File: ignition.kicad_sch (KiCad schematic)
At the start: 5 parts, among them J2 Centroid, Q1 Q_NMOS_GDS

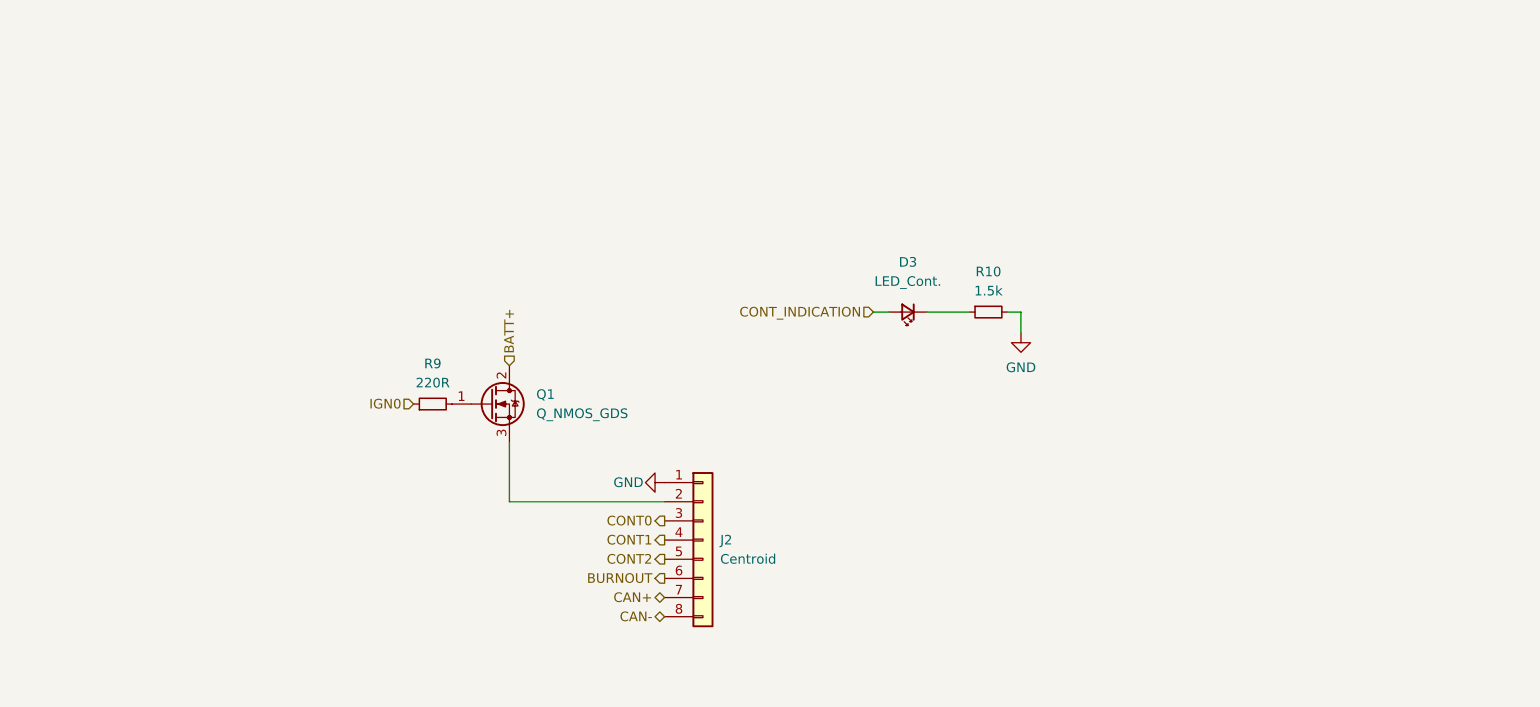
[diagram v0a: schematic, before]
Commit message: Update ignition system with CDI
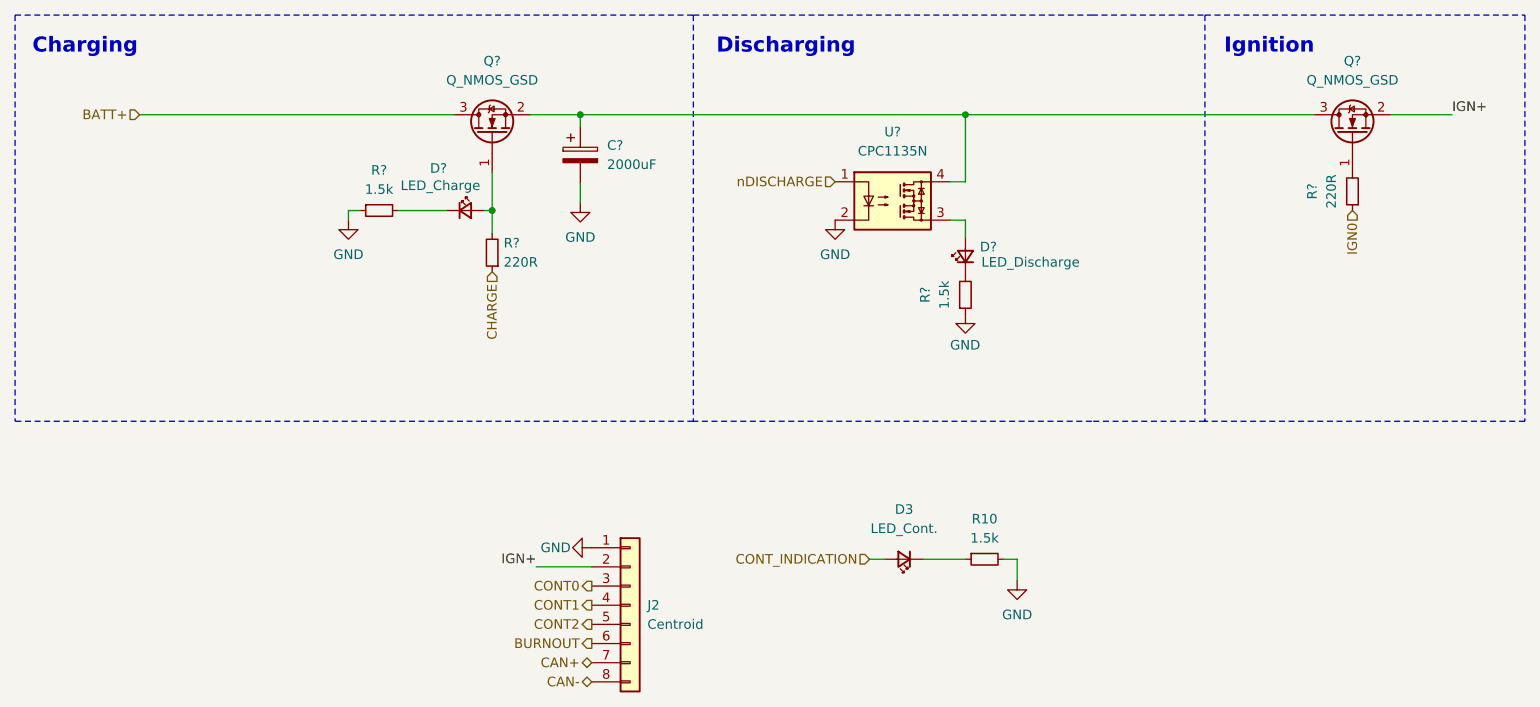
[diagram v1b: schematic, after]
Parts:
- removed Q1: Q_NMOS_GDS, Package_TO_SOT_SMD:TO-263-3_TabPin2, symbol Device:Q_NMOS_GDS
- removed R9: 220R, Resistor_SMD:R_0402_1005Metric, symbol Device:R_Small
- added C?: 2000uF, symbol Device:C_Polarized
- added D?: LED_Charge, LED_SMD:LED_0603_1608Metric, symbol Device:LED_Small
- added D?: LED_Discharge, LED_SMD:LED_0603_1608Metric, symbol Device:LED_Small
- added Q? (x2): Q_NMOS_GSD, symbol Device:Q_NMOS_GSD
- added R? (x2): 220R, Resistor_SMD:R_0402_1005Metric, symbol Device:R_Small
- added R? (x2): 1.5k, Resistor_SMD:R_0402_1005Metric, symbol Device:R_Small
- added U?: CPC1135N, Package_SO:SOP-4_3.8x4.1mm_P2.54mm, symbol Relay_SolidState:CPC1117N
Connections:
- net BATT+: now also Q?.3 (D)
- net GND: now also C?.2, R?.1, R?.1, U?.2
- net IGN0: now also R?.1
- net IGN+: now reaches J2.2 (Pin_2)
- net IGN+: now also Q?.2 (S)
- new net: D?.1 (K), R?.2 (x2)
- new net: D?.2 (A), Q?.1 (G), R?.2
- new net: D?.2 (A), U?.3
- new net: Q?.1 (G), R?.2
- new net: C?.1, Q?.2 (S), Q?.3 (D), U?.4
- new net CHARGE: R?.1
- new net nDISCHARGE: U?.1
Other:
- note added: "Charging"
- note added: "Discharging"
- note added: "Ignition"
- moved on the sheet: D3, J2, R10

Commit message: Finish Engine Control Rev2
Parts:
- C13: renamed from C?; footprint (none) -> Capacitor_THT:CP_Radial_D12.5mm_P5.00mm
- Q1, Q2: renamed from Q?; footprint (none) -> Package_TO_SOT_SMD:SOT-23
- gave numbers to parts that had none: 7
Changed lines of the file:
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@@
   (paper "A4")
   (junction (at 110.49 65.532) (diameter 0.9144) (color 0 0 0 0))
-  (junction (at 122.174 52.832) (diameter 0.9144) (color 0 0 0 0))
-  (junction (at 173.228 52.832) (diameter 0.9144) (color 0 0 0 0))
+  (junction (at 122.174 52.832) (diameter 2.4136) (color 0 0 0 0))
+  (junction (at 173.228 52.832) (diameter 2.4136) (color 0 0 0 0))
   (wire (pts (xy 63.754 52.832) (xy 105.41 52.832))
     (stroke (width 0) (type solid) (color 0 0 0 0))
@@
   )
   (wire (pts (xy 122.174 61.976) (xy 122.174 64.516))
+    (stroke (width 0) (type solid) (color 0 0 0 0))
+  )
+  (wire (pts (xy 122.174 110.236) (xy 123.698 110.236))
     (stroke (width 0) (type solid) (color 0 0 0 0))
   )
@@
   (symbol (lib_id "power:GND") (at 91.44 66.802 0) (unit 1)
     (in_bom yes) (on_board yes) (fields_autoplaced)
-    (property "Reference" "#PWR?" (id 0) (at 91.44 73.152 0)
+    (property "Reference" "#PWR022" (id 0) (at 91.44 73.152 0)
       (effects (font (size 1.27 1.27)) hide)
     )
@@
   (symbol (lib_id "power:GND") (at 122.174 64.516 0) (unit 1)
     (in_bom yes) (on_board yes) (fields_autoplaced)
-    (property "Reference" "#PWR?" (id 0) (at 122.174 70.866 0)
+    (property "Reference" "#PWR023" (id 0) (at 122.174 70.866 0)
       (effects (font (size 1.27 1.27)) hide)
     )
@@
     (pin "1")
   )
-  (symbol (lib_id "power:GND") (at 123.698 110.236 270) (unit 1)
+  (symbol (lib_id "power:GND") (at 122.174 110.236 270) (unit 1)
     (in_bom yes) (on_board yes)
-    (property "Reference" "#PWR019" (id 0) (at 117.348 110.236 0)
-      (effects (font (size 1.27 1.27)) hide)
-    )
-    (property "Value" "GND" (id 1) (at 120.904 110.2359 90)
+    (property "Reference" "#PWR019" (id 0) (at 115.824 110.236 0)
+      (effects (font (size 1.27 1.27)) hide)
+    )
+    (property "Value" "GND" (id 1) (at 119.38 110.2359 90)
       (effects (font (size 1.27 1.27)) (justify right))
     )
-    (property "Footprint" "" (id 2) (at 123.698 110.236 0)
-      (effects (font (size 1.27 1.27)) hide)
-    )
-    (property "Datasheet" "" (id 3) (at 123.698 110.236 0)
+    (property "Footprint" "" (id 2) (at 122.174 110.236 0)
+      (effects (font (size 1.27 1.27)) hide)
+    )
+    (property "Datasheet" "" (id 3) (at 122.174 110.236 0)
       (effects (font (size 1.27 1.27)) hide)
     )
@@
   (symbol (lib_id "power:GND") (at 155.956 66.802 0) (unit 1)
     (in_bom yes) (on_board yes) (fields_autoplaced)
-    (property "Reference" "#PWR?" (id 0) (at 155.956 73.152 0)
+    (property "Reference" "#PWR024" (id 0) (at 155.956 73.152 0)
       (effects (font (size 1.27 1.27)) hide)
     )
@@
   (symbol (lib_id "power:GND") (at 173.228 79.248 0) (unit 1)
     (in_bom yes) (on_board yes)
-    (property "Reference" "#PWR?" (id 0) (at 173.228 85.598 0)
+    (property "Reference" "#PWR025" (id 0) (at 173.228 85.598 0)
       (effects (font (size 1.27 1.27)) hide)
     )
@@
   (symbol (lib_id "Device:R_Small") (at 95.504 65.532 90) (mirror x) (unit 1)
     (in_bom yes) (on_board yes) (fields_autoplaced)
-    (property "Reference" "R?" (id 0) (at 95.504 60.198 90))
+    (property "Reference" "R9" (id 0) (at 95.504 60.198 90))
     (property "Value" "1.5k" (id 1) (at 95.504 62.738 90))
     (property "Footprint" "Resistor_SMD:R_0402_1005Metric" (id 2) (at 95.504 65.532 0)
@@
   (symbol (lib_id "Device:R_Small") (at 110.49 71.12 180) (unit 1)
     (in_bom yes) (on_board yes) (fields_autoplaced)
-    (property "Reference" "R?" (id 0) (at 112.014 69.8499 0)
+    (property "Reference" "R11" (id 0) (at 112.014 69.8499 0)
       (effects (font (size 1.27 1.27)) (justify right))
     )
@@
   (symbol (lib_id "Device:R_Small") (at 173.228 76.708 0) (mirror x) (unit 1)
     (in_bom yes) (on_board yes) (fields_autoplaced)
-    (property "Reference" "R?" (id 0) (at 167.894 76.708 90))
+    (property "Reference" "R12" (id 0) (at 167.894 76.708 90))
     (property "Value" "1.5k" (id 1) (at 170.434 76.708 90))
     (property "Footprint" "Resistor_SMD:R_0402_1005Metric" (id 2) (at 173.228 76.708 0)
@@
   (symbol (lib_id "Device:R_Small") (at 224.536 62.992 180) (unit 1)
     (in_bom yes) (on_board yes) (fields_autoplaced)
-    (property "Reference" "R?" (id 0) (at 219.202 62.992 90))
+    (property "Reference" "R13" (id 0) (at 219.202 62.992 90))
     (property "Value" "220R" (id 1) (at 221.742 62.992 90))
     (property "Footprint" "Resistor_SMD:R_0402_1005Metric" (id 2) (at 224.536 62.992 0)
@@
   (symbol (lib_id "Device:LED_Small") (at 106.934 65.532 0) (unit 1)
     (in_bom yes) (on_board yes)
-    (property "Reference" "D?" (id 0) (at 103.378 59.944 0))
+    (property "Reference" "D4" (id 0) (at 103.378 59.944 0))
     (property "Value" "LED_Charge" (id 1) (at 103.632 62.23 0))
     (property "Footprint" "LED_SMD:LED_0603_1608Metric" (id 2) (at 106.934 65.532 90)
@@
   (symbol (lib_id "Device:LED_Small") (at 173.228 71.628 90) (unit 1)
     (in_bom yes) (on_board yes)
-    (property "Reference" "D?" (id 0) (at 176.276 70.358 90))
+    (property "Reference" "D5" (id 0) (at 176.276 70.358 90))
     (property "Value" "LED_Discharge" (id 1) (at 181.864 72.39 90))
     (property "Footprint" "LED_SMD:LED_0603_1608Metric" (id 2) (at 173.228 71.628 90)
@@
   (symbol (lib_id "Device:C_Polarized") (at 122.174 58.166 0) (unit 1)
     (in_bom yes) (on_board yes) (fields_autoplaced)
-    (property "Reference" "C?" (id 0) (at 125.73 56.8959 0)
+    (property "Reference" "C13" (id 0) (at 125.73 56.8959 0)
       (effects (font (size 1.27 1.27)) (justify left))
     )
@@
       (effects (font (size 1.27 1.27)) (justify left))
     )
-    (property "Footprint" "" (id 2) (at 123.1392 61.976 0)
+    (property "Footprint" "Capacitor_THT:CP_Radial_D12.5mm_P5.00mm" (id 2) (at 123.1392 61.976 0)
       (effects (font (size 1.27 1.27)) hide)
     )
@@
   (symbol (lib_id "Device:Q_NMOS_GSD") (at 110.49 55.372 90) (unit 1)
     (in_bom yes) (on_board yes) (fields_autoplaced)
-    (property "Reference" "Q?" (id 0) (at 110.49 45.72 90))
+    (property "Reference" "Q1" (id 0) (at 110.49 45.72 90))
     (property "Value" "Q_NMOS_GSD" (id 1) (at 110.49 48.26 90))
-    (property "Footprint" "" (id 2) (at 107.95 50.292 0)
+    (property "Footprint" "Package_TO_SOT_SMD:SOT-23" (id 2) (at 107.95 50.292 0)
       (effects (font (size 1.27 1.27)) hide)
     )
@@
   (symbol (lib_id "Device:Q_NMOS_GSD") (at 224.536 55.372 90) (unit 1)
     (in_bom yes) (on_board yes) (fields_autoplaced)
-    (property "Reference" "Q?" (id 0) (at 224.536 45.72 90))
+    (property "Reference" "Q2" (id 0) (at 224.536 45.72 90))
     (property "Value" "Q_NMOS_GSD" (id 1) (at 224.536 48.26 90))
-    (property "Footprint" "" (id 2) (at 221.996 50.292 0)
+    (property "Footprint" "Package_TO_SOT_SMD:SOT-23" (id 2) (at 221.996 50.292 0)
       (effects (font (size 1.27 1.27)) hide)
     )
@@
   (symbol (lib_id "Relay_SolidState:CPC1117N") (at 163.576 64.262 0) (unit 1)
     (in_bom yes) (on_board yes) (fields_autoplaced)
-    (property "Reference" "U?" (id 0) (at 163.576 55.118 0))
+    (property "Reference" "U4" (id 0) (at 163.576 55.118 0))
     (property "Value" "CPC1135N" (id 1) (at 163.576 57.658 0))
     (property "Footprint" "Package_SO:SOP-4_3.8x4.1mm_P2.54mm" (id 2) (at 158.496 69.342 0)

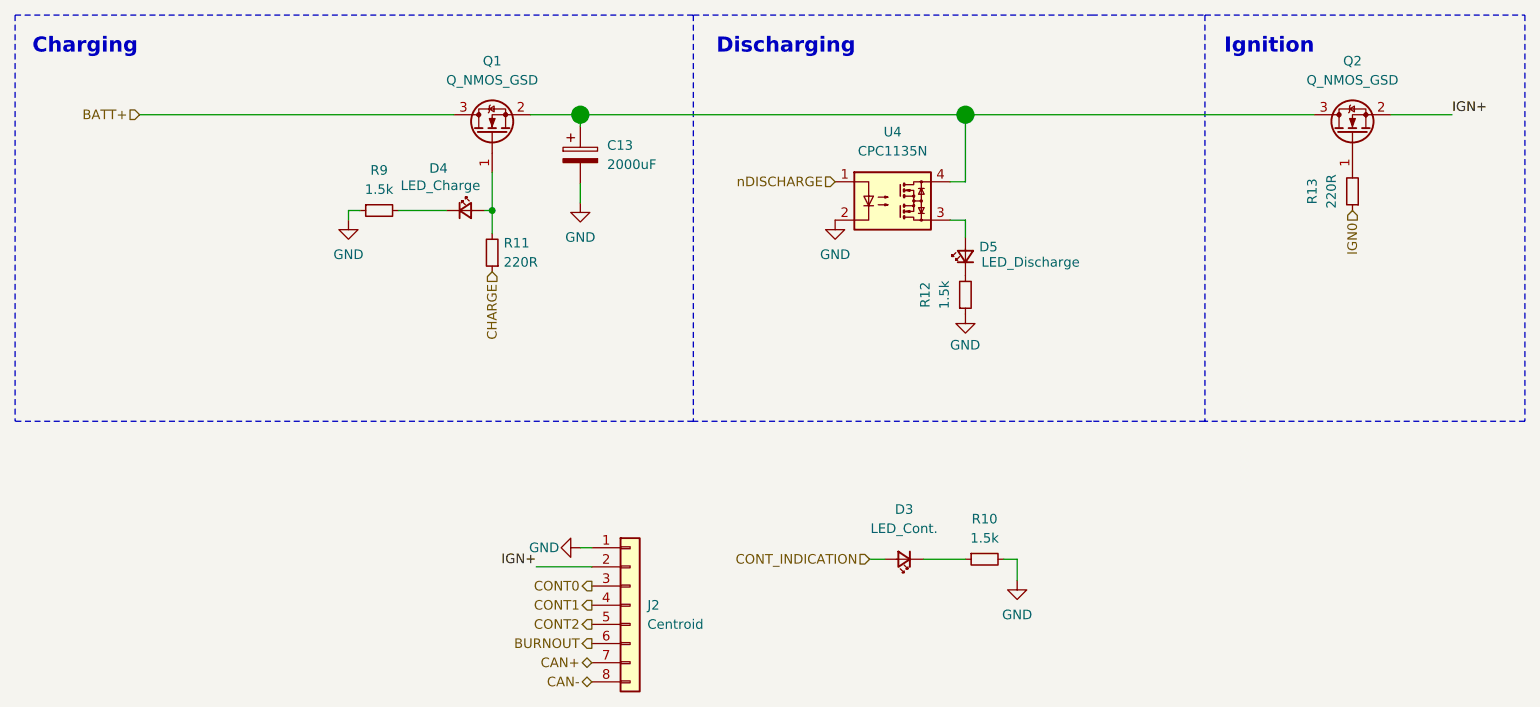
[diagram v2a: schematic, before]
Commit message: #4 add pchannel for charge and nchannel for ignition
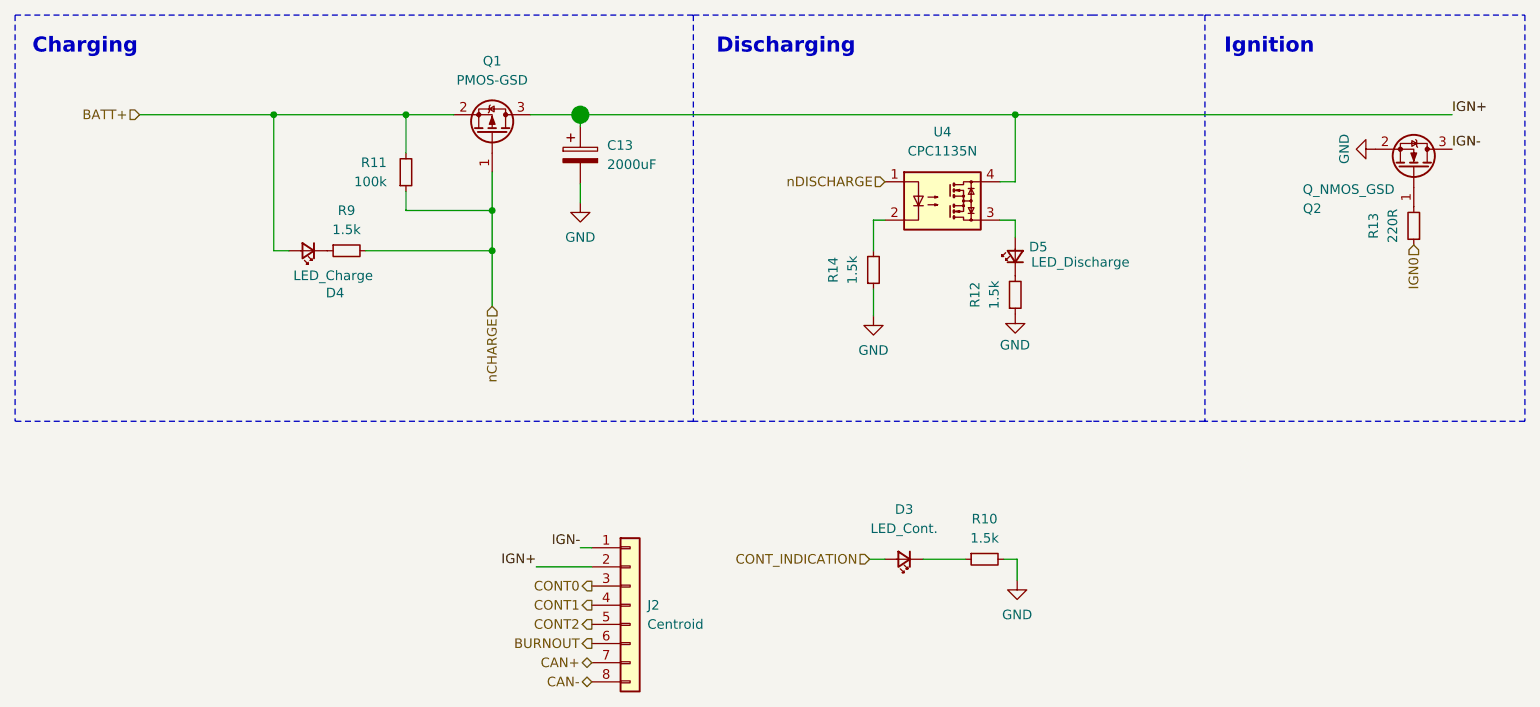
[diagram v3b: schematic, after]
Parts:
- removed Q1: Q_NMOS_GSD, Package_TO_SOT_SMD:SOT-23, symbol Device:Q_NMOS_GSD
- added Q1: PMOS-GSD, Package_TO_SOT_SMD:SOT-23, symbol Device:Q_PMOS_GSD
- added R14: 1.5k, Resistor_SMD:R_0402_1005Metric, symbol Device:R_Small
- R11: value 220R -> 100k; footprint Resistor_SMD:R_0402_1005Metric -> (none)
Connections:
- net BATT+: now also D4.2 (A), R11.2, Q1.2 (S)
- net GND: now also Q2.2 (S), R14.1; no longer J2.1 (Pin_1), R9.1, U4.2
- net IGN+: now also C13.1, U4.4, Q1.3 (D); no longer Q2.2 (S)
- net at D4.1 (K): now also R9.1; no longer R9.2
- net CHARGE renamed nCHARGE
- net nCHARGE: now also R9.2, Q1.1 (G)
- new net: R14.2, U4.2
- new net IGN-: J2.1 (Pin_1), Q2.3 (D)
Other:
- moved on the sheet: D4, D5, Q2, R12, R13, R9, U4
